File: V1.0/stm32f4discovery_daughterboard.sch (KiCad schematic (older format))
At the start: 67 parts, among them P1 CONN_25X2, P2 CONN_25X2, T1 BC547

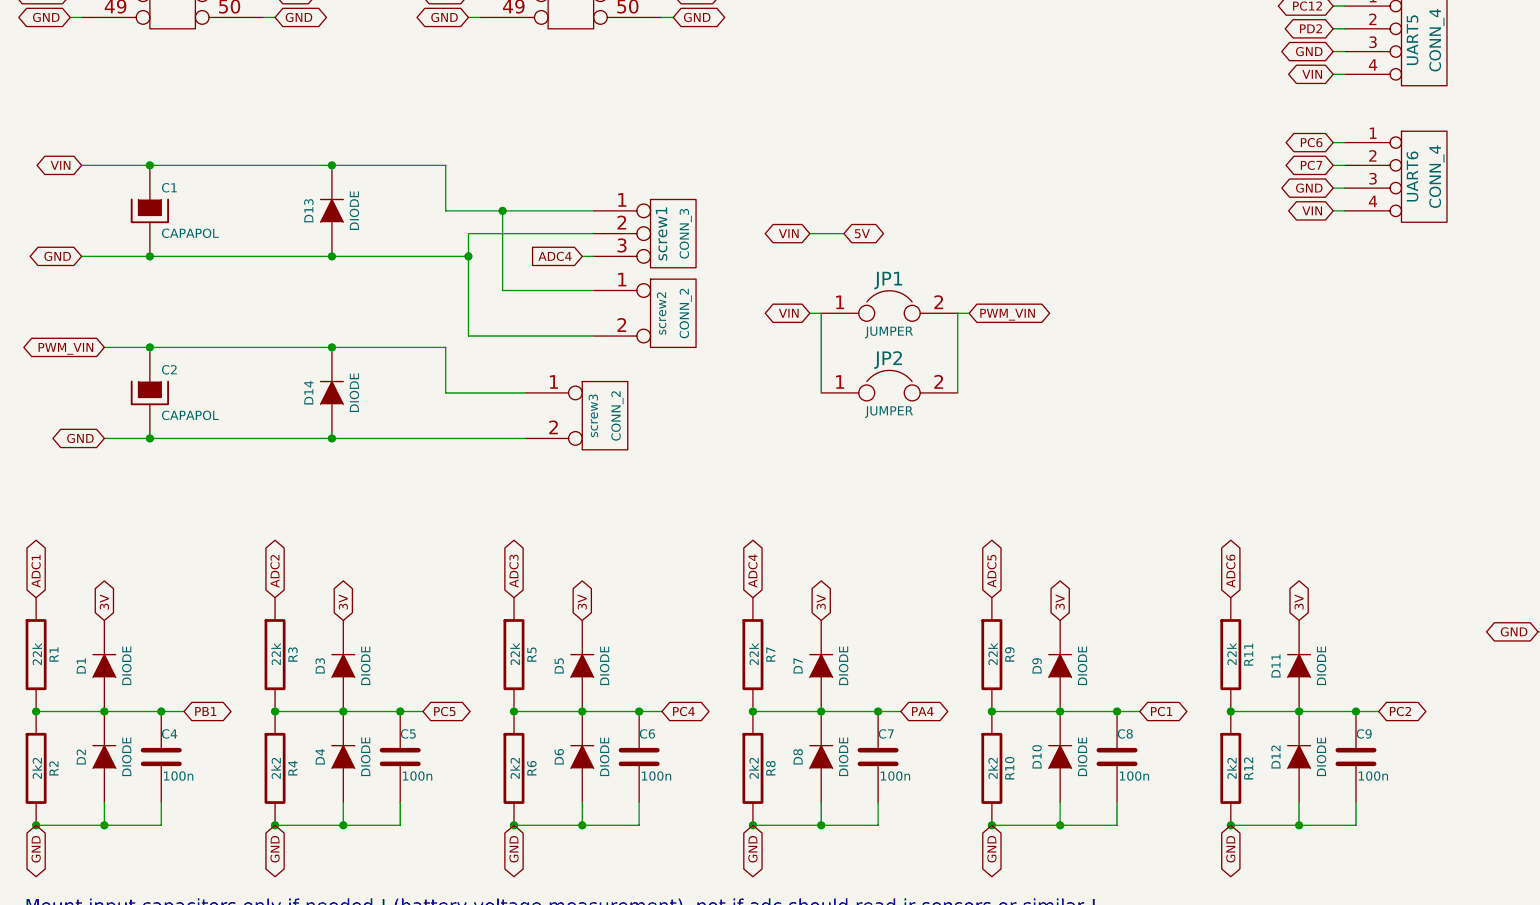
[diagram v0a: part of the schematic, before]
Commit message: added filter caps on input
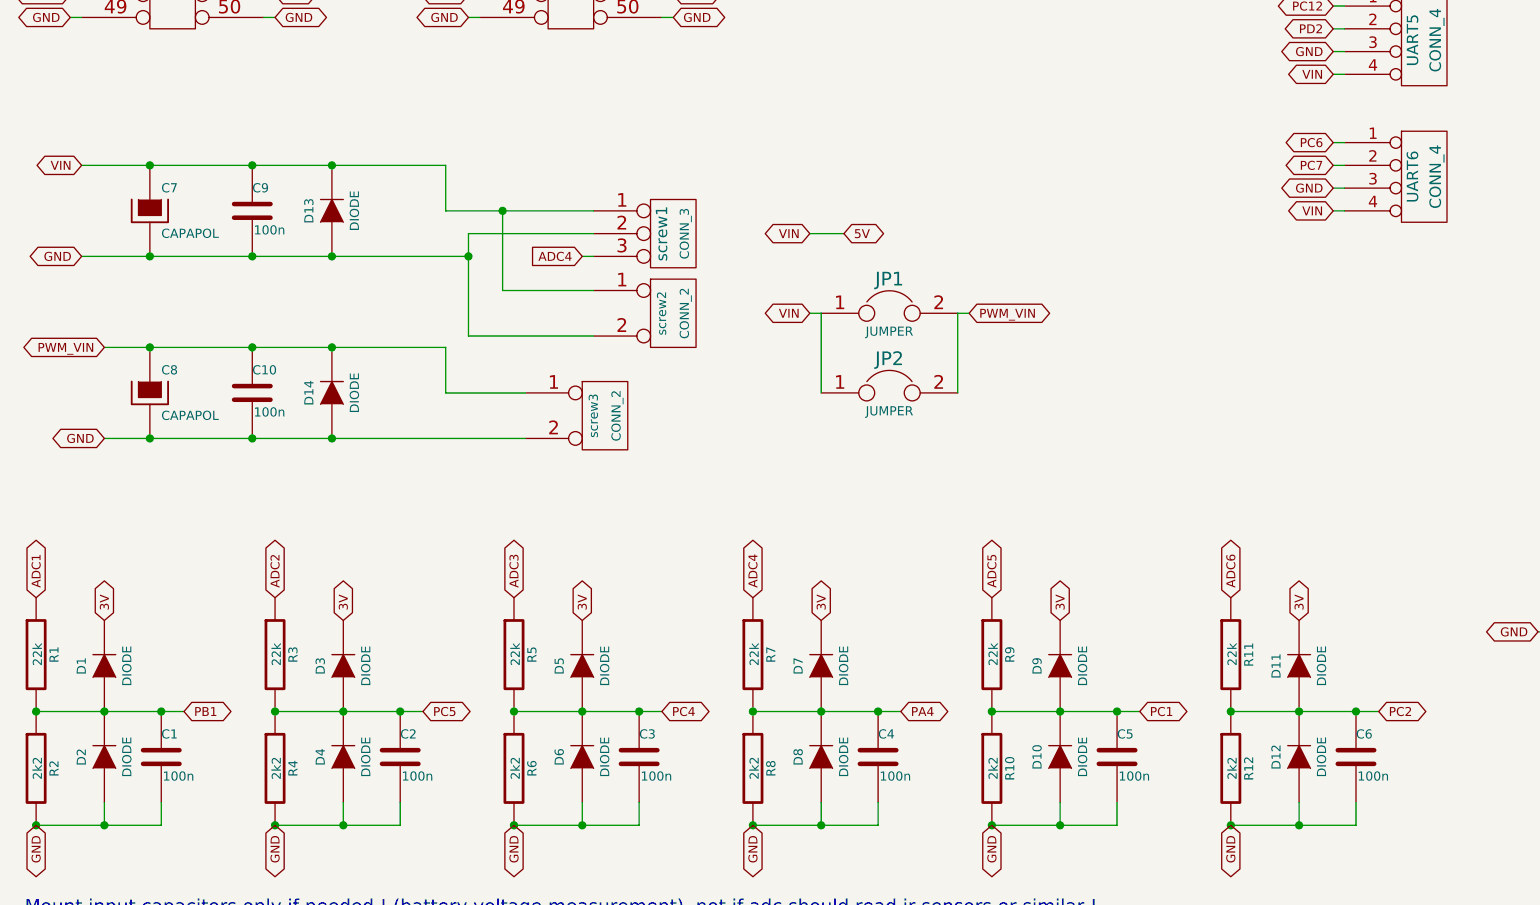
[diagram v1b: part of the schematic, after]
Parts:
- added C10, C9: 100n, C1, symbol C
- JP1, JP2: footprint SM1210 -> Ujumper
- renumbered C4 to C1, C5 to C2, C6 to C3, C7 to C4, C8 to C5, C9 to C6, C1 to C7, C2 to C8
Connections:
- net 5V: now also C9.1
- net GND: now also C10.2, C9.2
- net PWM_VIN: now also C10.1
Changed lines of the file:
@@
 Sheet 1 1
 Title "STM32F4 Discovery Daughterboard Paparazzi"
-Date "31 mar 2014"
+Date "7 apr 2014"
 Rev "V1.0"
 Comp ""
@@
 F 0 "JP1" H 4750 5000 60  0000 C CNN
 F 1 "JUMPER" H 4750 4770 40  0000 C CNN
-F 2 "SM1210" H 4750 4850 60  0001 C CNN
+F 2 "Ujumper" H 4750 4850 60  0001 C CNN
 F 3 "~" H 4750 4850 60  0000 C CNN
 	1    4750 4850
@@
 F 0 "JP2" H 4750 5350 60  0000 C CNN
 F 1 "JUMPER" H 4750 5120 40  0000 C CNN
-F 2 "SM1210" H 4750 5200 60  0001 C CNN
+F 2 "Ujumper" H 4750 5200 60  0001 C CNN
 F 3 "~" H 4750 5200 60  0000 C CNN
 	1    4750 5200
@@
 $EndComp
 $Comp
-L CAPAPOL C2
+L CAPAPOL C8
 U 1 1 53308663
 P 1500 5200
-F 0 "C2" H 1550 5300 40  0000 L CNN
+F 0 "C8" H 1550 5300 40  0000 L CNN
 F 1 "CAPAPOL" H 1550 5100 40  0000 L CNN
 F 2 "C2V8" H 1600 5050 30  0001 C CNN
@@
 $EndComp
 $Comp
-L CAPAPOL C1
+L CAPAPOL C7
 U 1 1 53308676
 P 1500 4400
-F 0 "C1" H 1550 4500 40  0000 L CNN
+F 0 "C7" H 1550 4500 40  0000 L CNN
 F 1 "CAPAPOL" H 1550 4300 40  0000 L CNN
 F 2 "C2V8" H 1600 4250 30  0001 C CNN
@@
 VIN
 $Comp
-L C C5
+L C C2
 U 1 1 5331FFE7
 P 2600 6800
-F 0 "C5" H 2600 6900 40  0000 L CNN
+F 0 "C2" H 2600 6900 40  0000 L CNN
 F 1 "100n" H 2606 6715 40  0000 L CNN
 F 2 "C1" H 2638 6650 30  0001 C CNN
@@
 ADC4
 $Comp
-L C C4
+L C C1
 U 1 1 5334159B
 P 1550 6800
-F 0 "C4" H 1550 6900 40  0000 L CNN
+F 0 "C1" H 1550 6900 40  0000 L CNN
 F 1 "100n" H 1556 6715 40  0000 L CNN
 F 2 "C1" H 1588 6650 30  0001 C CNN
@@
 $EndComp
 $Comp
-L C C6
+L C C3
 U 1 1 533415A1
 P 3650 6800
-F 0 "C6" H 3650 6900 40  0000 L CNN
+F 0 "C3" H 3650 6900 40  0000 L CNN
 F 1 "100n" H 3656 6715 40  0000 L CNN
 F 2 "C1" H 3688 6650 30  0001 C CNN
@@
 $EndComp
 $Comp
-L C C7
+L C C4
 U 1 1 533415A7
 P 4700 6800
-F 0 "C7" H 4700 6900 40  0000 L CNN
+F 0 "C4" H 4700 6900 40  0000 L CNN
 F 1 "100n" H 4706 6715 40  0000 L CNN
 F 2 "C1" H 4738 6650 30  0001 C CNN
@@
 $EndComp
 $Comp
-L C C8
+L C C5
 U 1 1 533415AD
 P 5750 6800
-F 0 "C8" H 5750 6900 40  0000 L CNN
+F 0 "C5" H 5750 6900 40  0000 L CNN
 F 1 "100n" H 5756 6715 40  0000 L CNN
 F 2 "C1" H 5788 6650 30  0001 C CNN
@@
 $EndComp
 $Comp
-L C C9
+L C C6
 U 1 1 533415B3
 P 6800 6800
-F 0 "C9" H 6800 6900 40  0000 L CNN
+F 0 "C6" H 6800 6900 40  0000 L CNN
 F 1 "100n" H 6806 6715 40  0000 L CNN
 F 2 "C1" H 6838 6650 30  0001 C CNN
@@
 	1    0    0    -1
 $EndComp
+$Comp
+L C C9
+U 1 1 53430CB7
+P 1950 4400
+F 0 "C9" H 1950 4500 40  0000 L CNN
+F 1 "100n" H 1956 4315 40  0000 L CNN
+F 2 "C1" H 1988 4250 30  0001 C CNN
+F 3 "~" H 1950 4400 60  0000 C CNN
+	1    1950 4400
+	1    0    0    -1
+$EndComp
+$Comp
+L C C10
+U 1 1 53430CBD
+P 1950 5200
+F 0 "C10" H 1950 5300 40  0000 L CNN
+F 1 "100n" H 1956 5115 40  0000 L CNN
+F 2 "C1" H 1988 5050 30  0001 C CNN
+F 3 "~" H 1950 5200 60  0000 C CNN
+	1    1950 5200
+	1    0    0    -1
+$EndComp
+Connection ~ 1950 4200
+Connection ~ 1950 4600
+Connection ~ 1950 5000
+Connection ~ 1950 5400
 $EndSCHEMATC

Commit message: final v1.0
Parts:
- D1, D10, D11, D12, D13, D14, D15, D2, D3, D4, D5, D6, D7, D8, D9: footprint D3 -> do41_modified
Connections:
- net Pb9 is gone; now on net PB9: I2C1.2 (P2)
- net 3V: now also BOOT0.1
- net GND: no longer BOOT0.1
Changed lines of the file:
@@
 Sheet 1 1
 Title "STM32F4 Discovery Daughterboard Paparazzi"
-Date "7 apr 2014"
+Date "11 apr 2014"
 Rev "V1.0"
 Comp ""
@@
 Text GLabel 2900 2050 0    39   BiDi ~ 0
 PB8
-Text GLabel 2900 2150 0    39   Input ~ 0
+Text GLabel 2900 2150 0    39   BiDi ~ 0
 BOOT0
 Text GLabel 2900 2250 0    39   BiDi ~ 0
@@
 	1    0    0    -1
 $EndComp
-Text GLabel 7600 6250 0    39   BiDi ~ 0
-GND
 Text GLabel 8300 6250 2    39   BiDi ~ 0
 BOOT0
@@
 F 0 "D1" H 1300 6500 40  0000 C CNN
 F 1 "DIODE" H 1300 6300 40  0000 C CNN
-F 2 "D3" H 1300 6400 60  0001 C CNN
+F 2 "do41_modified" H 1300 6400 60  0001 C CNN
 F 3 "~" H 1300 6400 60  0000 C CNN
 	1    1300 6400
@@
 F 0 "D2" H 1300 6900 40  0000 C CNN
 F 1 "DIODE" H 1300 6700 40  0000 C CNN
-F 2 "D3" H 1300 6800 60  0001 C CNN
+F 2 "do41_modified" H 1300 6800 60  0001 C CNN
 F 3 "~" H 1300 6800 60  0000 C CNN
 	1    1300 6800
@@
 F 0 "D3" H 2350 6500 40  0000 C CNN
 F 1 "DIODE" H 2350 6300 40  0000 C CNN
-F 2 "D3" H 2350 6400 60  0001 C CNN
+F 2 "do41_modified" H 2350 6400 60  0001 C CNN
 F 3 "~" H 2350 6400 60  0000 C CNN
 	1    2350 6400
@@
 F 0 "D4" H 2350 6900 40  0000 C CNN
 F 1 "DIODE" H 2350 6700 40  0000 C CNN
-F 2 "D3" H 2350 6800 60  0001 C CNN
+F 2 "do41_modified" H 2350 6800 60  0001 C CNN
 F 3 "~" H 2350 6800 60  0000 C CNN
 	1    2350 6800
@@
 F 0 "D5" H 3400 6500 40  0000 C CNN
 F 1 "DIODE" H 3400 6300 40  0000 C CNN
-F 2 "D3" H 3400 6400 60  0001 C CNN
+F 2 "do41_modified" H 3400 6400 60  0001 C CNN
 F 3 "~" H 3400 6400 60  0000 C CNN
 	1    3400 6400
@@
 F 0 "D6" H 3400 6900 40  0000 C CNN
 F 1 "DIODE" H 3400 6700 40  0000 C CNN
-F 2 "D3" H 3400 6800 60  0001 C CNN
+F 2 "do41_modified" H 3400 6800 60  0001 C CNN
 F 3 "~" H 3400 6800 60  0000 C CNN
 	1    3400 6800
@@
 F 0 "D7" H 4450 6500 40  0000 C CNN
 F 1 "DIODE" H 4450 6300 40  0000 C CNN
-F 2 "D3" H 4450 6400 60  0001 C CNN
+F 2 "do41_modified" H 4450 6400 60  0001 C CNN
 F 3 "~" H 4450 6400 60  0000 C CNN
 	1    4450 6400
@@
 F 0 "D8" H 4450 6900 40  0000 C CNN
 F 1 "DIODE" H 4450 6700 40  0000 C CNN
-F 2 "D3" H 4450 6800 60  0001 C CNN
+F 2 "do41_modified" H 4450 6800 60  0001 C CNN
 F 3 "~" H 4450 6800 60  0000 C CNN
 	1    4450 6800
@@
 F 0 "D9" H 5500 6500 40  0000 C CNN
 F 1 "DIODE" H 5500 6300 40  0000 C CNN
-F 2 "D3" H 5500 6400 60  0001 C CNN
+F 2 "do41_modified" H 5500 6400 60  0001 C CNN
 F 3 "~" H 5500 6400 60  0000 C CNN
 	1    5500 6400
@@
 F 0 "D10" H 5500 6900 40  0000 C CNN
 F 1 "DIODE" H 5500 6700 40  0000 C CNN
-F 2 "D3" H 5500 6800 60  0001 C CNN
+F 2 "do41_modified" H 5500 6800 60  0001 C CNN
 F 3 "~" H 5500 6800 60  0000 C CNN
 	1    5500 6800
@@
 F 0 "D11" H 6550 6500 40  0000 C CNN
 F 1 "DIODE" H 6550 6300 40  0000 C CNN
-F 2 "D3" H 6550 6400 60  0001 C CNN
+F 2 "do41_modified" H 6550 6400 60  0001 C CNN
 F 3 "~" H 6550 6400 60  0000 C CNN
 	1    6550 6400
@@
 F 0 "D12" H 6550 6900 40  0000 C CNN
 F 1 "DIODE" H 6550 6700 40  0000 C CNN
-F 2 "D3" H 6550 6800 60  0001 C CNN
+F 2 "do41_modified" H 6550 6800 60  0001 C CNN
 F 3 "~" H 6550 6800 60  0000 C CNN
 	1    6550 6800
@@
 PB8
 Text GLabel 7750 1200 0    39   BiDi ~ 0
-Pb9
+PB9
 Text GLabel 7750 1700 0    39   BiDi ~ 0
 PB10
@@
 F 0 "D13" H 2300 4500 40  0000 C CNN
 F 1 "DIODE" H 2300 4300 40  0000 C CNN
-F 2 "D3" H 2300 4400 60  0001 C CNN
+F 2 "do41_modified" H 2300 4400 60  0001 C CNN
 F 3 "~" H 2300 4400 60  0000 C CNN
 	1    2300 4400
@@
 F 0 "D15" H 5100 2400 40  0000 C CNN
 F 1 "DIODE" H 5100 2200 40  0000 C CNN
-F 2 "D3" H 5100 2300 60  0001 C CNN
+F 2 "do41_modified" H 5100 2300 60  0001 C CNN
 F 3 "~" H 5100 2300 60  0000 C CNN
 	1    5100 2300
@@
 F 0 "D14" H 2300 5300 40  0000 C CNN
 F 1 "DIODE" H 2300 5100 40  0000 C CNN
-F 2 "D3" H 2300 5200 60  0001 C CNN
+F 2 "do41_modified" H 2300 5200 60  0001 C CNN
 F 3 "~" H 2300 5200 60  0000 C CNN
 	1    2300 5200
@@
 Connection ~ 1950 5000
 Connection ~ 1950 5400
+Text GLabel 7600 6250 0    39   BiDi ~ 0
+3V
 $EndSCHEMATC
